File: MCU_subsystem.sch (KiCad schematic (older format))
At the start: 14 parts, among them U3 MX25R8035FZUIL0, U601 cc1352p, Y601 32.768kHz, Y602 48MHz

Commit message: relinked LED and BTN footprints. Need to make flash symbol again
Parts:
- U3: symbol FLASH:MX25R8035FZUIL0 -> UserMade-BB-Zigbee-Gateway-CAPE:MX25R8035FZUIL0
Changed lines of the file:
@@
 	2900 5950 2700 5950
 $Comp
-L FLASH:MX25R8035FZUIL0 U3
+L UserMade-BB-Zigbee-Gateway-CAPE:MX25R8035FZUIL0 U3
 U 1 1 615019E6
 P 4300 6700

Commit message: Recovered the .lib for flash symbol. Relinked in schematic
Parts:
- C26, C601, C602: symbol Device:C -> BeagleBone-Black-Cape-rescue:C-Device
- C603, C604: symbol pspice:CAP -> BeagleBone-Black-Cape-rescue:CAP-pspice
- R14, R15, R16, R17, R601: symbol Device:R_US -> BeagleBone-Black-Cape-rescue:R_US-Device
- U3: symbol UserMade-BB-Zigbee-Gateway-CAPE:MX25R8035FZUIL0 -> Flash_Usr:MX25R8035FZUIL0
- Y601: symbol Device:Crystal -> BeagleBone-Black-Cape-rescue:Crystal-Device
- Y602: symbol Device:Crystal_GND2 -> BeagleBone-Black-Cape-rescue:Crystal_GND2-Device
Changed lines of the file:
@@
 SKY_V1_20DBM
 $Comp
-L power:GND #PWR0602
+L BeagleBone-Black-Cape-rescue:GND-power #PWR0602
 U 1 1 614C8FCE
 P 2150 4200
@@
 	2750 4100 2650 4100
 $Comp
-L Device:R_US R601
+L BeagleBone-Black-Cape-rescue:R_US-Device R601
 U 1 1 614CB248
 P 1700 3650
@@
 Connection ~ 2000 3800
 $Comp
-L Device:C C602
+L BeagleBone-Black-Cape-rescue:C-Device C602
 U 1 1 614CF3BD
 P 2150 4050
@@
 Connection ~ 1700 3400
 $Comp
-L Device:C C601
+L BeagleBone-Black-Cape-rescue:C-Device C601
 U 1 1 614D5273
 P 2050 3000
@@
 $EndComp
 $Comp
-L power:GND #PWR0601
+L BeagleBone-Black-Cape-rescue:GND-power #PWR0601
 U 1 1 614D592A
 P 2050 3150
@@
 	1700 2850 2050 2850
 $Comp
-L power:GND #PWR0603
+L BeagleBone-Black-Cape-rescue:GND-power #PWR0603
 U 1 1 614DC14A
 P 3150 5100
@@
 	3400 5100 3400 5000
 $Comp
-L Device:Crystal Y?
+L BeagleBone-Black-Cape-rescue:Crystal-Device Y?
 U 1 1 614E7AAF
 P 7450 4000
@@
 $EndComp
 $Comp
-L Device:Crystal_GND2 Y?
+L BeagleBone-Black-Cape-rescue:Crystal_GND2-Device Y?
 U 1 1 614E7AB5
 P 8750 4300
@@
 $EndComp
 $Comp
-L pspice:CAP C?
+L BeagleBone-Black-Cape-rescue:CAP-pspice C?
 U 1 1 614E7ABB
 P 7100 4350
@@
 $EndComp
 $Comp
-L pspice:CAP C?
+L BeagleBone-Black-Cape-rescue:CAP-pspice C?
 U 1 1 614E7AC1
 P 7800 4350
@@
 	7800 4000 7800 4100
 $Comp
-L power:GND #PWR?
+L BeagleBone-Black-Cape-rescue:GND-power #PWR?
 U 1 1 614E7ACB
 P 8750 4600
@@
 $EndComp
 $Comp
-L power:GND #PWR?
+L BeagleBone-Black-Cape-rescue:GND-power #PWR?
 U 1 1 614E7AD1
 P 7800 4700
@@
 $EndComp
 $Comp
-L power:GND #PWR?
+L BeagleBone-Black-Cape-rescue:GND-power #PWR?
 U 1 1 614E7AD7
 P 7100 4700
@@
 Exact cap Value will need to be \ndetermined by measuring the board. \nThis will also affect the exact \ncrystal we end up getting.
 $Comp
-L power:GND #PWR0143
+L BeagleBone-Black-Cape-rescue:GND-power #PWR0143
 U 1 1 614D787A
 P 4500 7100
@@
 $EndComp
 $Comp
-L power:GND #PWR0144
+L BeagleBone-Black-Cape-rescue:GND-power #PWR0144
 U 1 1 614D8142
 P 5100 7100
@@
 MCU_VDD
 $Comp
-L Device:R_US R16
+L BeagleBone-Black-Cape-rescue:R_US-Device R16
 U 1 1 614D91BC
 P 3450 6100
@@
 	3200 5950 3450 5950
 $Comp
-L Device:R_US R17
+L BeagleBone-Black-Cape-rescue:R_US-Device R17
 U 1 1 614DDC0C
 P 4950 6100
@@
 $EndComp
 $Comp
-L Device:C C26
+L BeagleBone-Black-Cape-rescue:C-Device C26
 U 1 1 614E11ED
 P 5100 6950
@@
 	3700 6500 3800 6500
 $Comp
-L Device:R_US R14
+L BeagleBone-Black-Cape-rescue:R_US-Device R14
 U 1 1 614EF3D8
 P 2900 6300
@@
 $EndComp
 $Comp
-L Device:R_US R15
+L BeagleBone-Black-Cape-rescue:R_US-Device R15
 U 1 1 614F0C42
 P 3200 6300
@@
 	2900 5950 2700 5950
 $Comp
-L UserMade-BB-Zigbee-Gateway-CAPE:MX25R8035FZUIL0 U3
+L Flash_Usr:MX25R8035FZUIL0 U3
 U 1 1 615019E6
 P 4300 6700

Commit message: prepped for PSU subsystem placements
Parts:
- U602: renamed from U3; symbol Flash_Usr:MX25R8035FZUIL0 -> BeagleBone-Black-Cape-rescue:MX25R8035FZUIL0-Flash_Usr
- renumbered C26 to C603, C603 to C604, C604 to C605, R14 to R602, R15 to R603, R16 to R604, R17 to R605
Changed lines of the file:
@@
 P 7100 4350
 AR Path="/613805C9/614E7ABB" Ref="C?"  Part="1"
-AR Path="/614C2CA1/614E7ABB" Ref="C603"  Part="1"
-F 0 "C603" H 7278 4396 50  0000 L CNN
+AR Path="/614C2CA1/614E7ABB" Ref="C604"  Part="1"
+F 0 "C604" H 7278 4396 50  0000 L CNN
 F 1 "CAP" H 7278 4305 50  0000 L CNN
 F 2 "Capacitor_SMD:C_0805_2012Metric_Pad1.18x1.45mm_HandSolder" H 7100 4350 50  0001 C CNN
@@
 P 7800 4350
 AR Path="/613805C9/614E7AC1" Ref="C?"  Part="1"
-AR Path="/614C2CA1/614E7AC1" Ref="C604"  Part="1"
-F 0 "C604" H 7978 4396 50  0000 L CNN
+AR Path="/614C2CA1/614E7AC1" Ref="C605"  Part="1"
+F 0 "C605" H 7978 4396 50  0000 L CNN
 F 1 "CAP" H 7978 4305 50  0000 L CNN
 F 2 "Capacitor_SMD:C_0805_2012Metric_Pad1.18x1.45mm_HandSolder" H 7800 4350 50  0001 C CNN
@@
 P 8750 4600
 AR Path="/613805C9/614E7ACB" Ref="#PWR?"  Part="1"
-AR Path="/614C2CA1/614E7ACB" Ref="#PWR0606"  Part="1"
-F 0 "#PWR0606" H 8750 4350 50  0001 C CNN
+AR Path="/614C2CA1/614E7ACB" Ref="#PWR0608"  Part="1"
+F 0 "#PWR0608" H 8750 4350 50  0001 C CNN
 F 1 "GND" H 8755 4427 50  0000 C CNN
 F 2 "" H 8750 4600 50  0001 C CNN
@@
 P 7800 4700
 AR Path="/613805C9/614E7AD1" Ref="#PWR?"  Part="1"
-AR Path="/614C2CA1/614E7AD1" Ref="#PWR0605"  Part="1"
-F 0 "#PWR0605" H 7800 4450 50  0001 C CNN
+AR Path="/614C2CA1/614E7AD1" Ref="#PWR0607"  Part="1"
+F 0 "#PWR0607" H 7800 4450 50  0001 C CNN
 F 1 "GND" H 7805 4527 50  0000 C CNN
 F 2 "" H 7800 4700 50  0001 C CNN
@@
 P 7100 4700
 AR Path="/613805C9/614E7AD7" Ref="#PWR?"  Part="1"
-AR Path="/614C2CA1/614E7AD7" Ref="#PWR0604"  Part="1"
-F 0 "#PWR0604" H 7100 4450 50  0001 C CNN
+AR Path="/614C2CA1/614E7AD7" Ref="#PWR0606"  Part="1"
+F 0 "#PWR0606" H 7100 4450 50  0001 C CNN
 F 1 "GND" H 7105 4527 50  0000 C CNN
 F 2 "" H 7100 4700 50  0001 C CNN
@@
 Exact cap Value will need to be \ndetermined by measuring the board. \nThis will also affect the exact \ncrystal we end up getting.
 $Comp
-L BeagleBone-Black-Cape-rescue:GND-power #PWR0143
+L BeagleBone-Black-Cape-rescue:GND-power #PWR0604
 U 1 1 614D787A
 P 4500 7100
-F 0 "#PWR0143" H 4500 6850 50  0001 C CNN
+F 0 "#PWR0604" H 4500 6850 50  0001 C CNN
 F 1 "GND" H 4505 6927 50  0000 C CNN
 F 2 "" H 4500 7100 50  0001 C CNN
@@
 $EndComp
 $Comp
-L BeagleBone-Black-Cape-rescue:GND-power #PWR0144
+L BeagleBone-Black-Cape-rescue:GND-power #PWR0605
 U 1 1 614D8142
 P 5100 7100
-F 0 "#PWR0144" H 5100 6850 50  0001 C CNN
+F 0 "#PWR0605" H 5100 6850 50  0001 C CNN
 F 1 "GND" H 5105 6927 50  0000 C CNN
 F 2 "" H 5100 7100 50  0001 C CNN
@@
 MCU_VDD
 $Comp
-L BeagleBone-Black-Cape-rescue:R_US-Device R16
+L BeagleBone-Black-Cape-rescue:R_US-Device R604
 U 1 1 614D91BC
 P 3450 6100
-F 0 "R16" H 3518 6146 50  0000 L CNN
+F 0 "R604" H 3518 6146 50  0000 L CNN
 F 1 "2.2k" H 3518 6055 50  0000 L CNN
 F 2 "Resistor_SMD:R_0805_2012Metric_Pad1.20x1.40mm_HandSolder" V 3490 6090 50  0001 C CNN
@@
 	3200 5950 3450 5950
 $Comp
-L BeagleBone-Black-Cape-rescue:R_US-Device R17
+L BeagleBone-Black-Cape-rescue:R_US-Device R605
 U 1 1 614DDC0C
 P 4950 6100
-F 0 "R17" H 5018 6146 50  0000 L CNN
+F 0 "R605" H 5018 6146 50  0000 L CNN
 F 1 "0" H 5018 6055 50  0000 L CNN
 F 2 "Resistor_SMD:R_0805_2012Metric_Pad1.20x1.40mm_HandSolder" V 4990 6090 50  0001 C CNN
@@
 $EndComp
 $Comp
-L BeagleBone-Black-Cape-rescue:C-Device C26
+L BeagleBone-Black-Cape-rescue:C-Device C603
 U 1 1 614E11ED
 P 5100 6950
-F 0 "C26" H 5215 6996 50  0000 L CNN
+F 0 "C603" H 5215 6996 50  0000 L CNN
 F 1 "0.1u" H 5215 6905 50  0000 L CNN
 F 2 "Capacitor_SMD:C_0805_2012Metric_Pad1.18x1.45mm_HandSolder" H 5138 6800 50  0001 C CNN
@@
 	3700 6500 3800 6500
 $Comp
-L BeagleBone-Black-Cape-rescue:R_US-Device R14
+L BeagleBone-Black-Cape-rescue:R_US-Device R602
 U 1 1 614EF3D8
 P 2900 6300
-F 0 "R14" H 2968 6346 50  0000 L CNN
+F 0 "R602" H 2968 6346 50  0000 L CNN
 F 1 "DNS" H 2968 6255 50  0000 L CNN
 F 2 "Resistor_SMD:R_0805_2012Metric_Pad1.20x1.40mm_HandSolder" V 2940 6290 50  0001 C CNN
@@
 $EndComp
 $Comp
-L BeagleBone-Black-Cape-rescue:R_US-Device R15
+L BeagleBone-Black-Cape-rescue:R_US-Device R603
 U 1 1 614F0C42
 P 3200 6300
-F 0 "R15" H 3268 6346 50  0000 L CNN
+F 0 "R603" H 3268 6346 50  0000 L CNN
 F 1 "DNS" H 3268 6255 50  0000 L CNN
 F 2 "Resistor_SMD:R_0805_2012Metric_Pad1.20x1.40mm_HandSolder" V 3240 6290 50  0001 C CNN
@@
 	2900 5950 2700 5950
 $Comp
-L Flash_Usr:MX25R8035FZUIL0 U3
+L BeagleBone-Black-Cape-rescue:MX25R8035FZUIL0-Flash_Usr U?
 U 1 1 615019E6
 P 4300 6700
-F 0 "U3" H 4844 6746 50  0000 L CNN
+AR Path="/615019E6" Ref="U?"  Part="1"
+AR Path="/614C2CA1/615019E6" Ref="U602"  Part="1"
+F 0 "U602" H 4844 6746 50  0000 L CNN
 F 1 "MX25R8035FZUIL0" H 4844 6655 50  0000 L CNN
 F 2 "Package_SO:SOP-8_5.28x5.23mm_P1.27mm" H 4300 6100 50  0001 C CNN

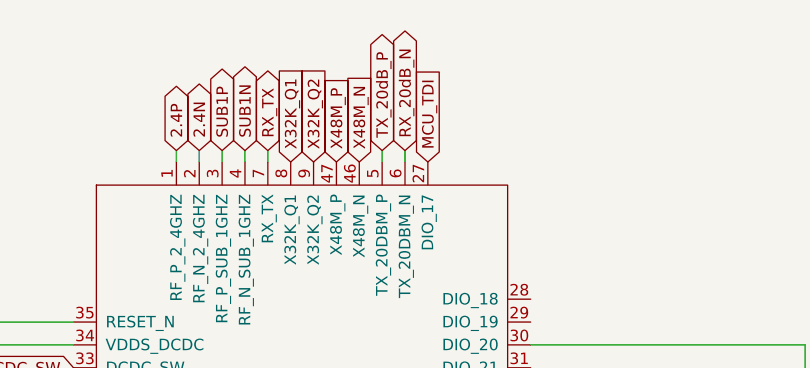
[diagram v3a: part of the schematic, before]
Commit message: Massive PCB/Schematic Update
The PCB has been completed, and the schematic has been updated to have the correct footprints
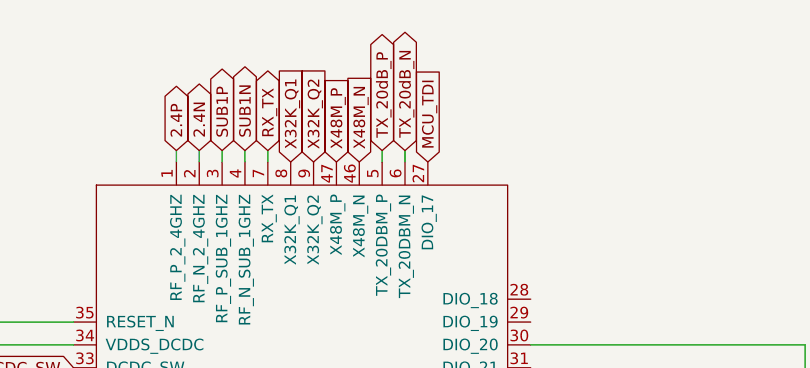
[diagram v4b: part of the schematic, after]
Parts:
- C601, C602: footprint Capacitor_SMD:C_0805_2012Metric_Pad1.18x1.45mm_HandSolder -> Capacitor_SMD:C_0402_1005Metric_Pad0.74x0.62mm_HandSolder
- R601: footprint Resistor_SMD:R_0805_2012Metric_Pad1.20x1.40mm_HandSolder -> Resistor_SMD:R_0402_1005Metric_Pad0.72x0.64mm_HandSolder
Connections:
- net RX_20dB_N renamed TX_20dB_N
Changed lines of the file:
@@
 	4200 2700 4200 2650
 Text GLabel 4300 2650 1    50   BiDi ~ 0
-RX_20dB_N
+TX_20dB_N
 Wire Wire Line
 	4300 2650 4300 2700
@@
 F 0 "R601" H 1768 3696 50  0000 L CNN
 F 1 "100k" H 1768 3605 50  0000 L CNN
-F 2 "Resistor_SMD:R_0805_2012Metric_Pad1.20x1.40mm_HandSolder" V 1740 3640 50  0001 C CNN
+F 2 "Resistor_SMD:R_0402_1005Metric_Pad0.72x0.64mm_HandSolder" V 1740 3640 50  0001 C CNN
 F 3 "~" H 1700 3650 50  0001 C CNN
 	1    1700 3650
@@
 F 0 "C602" H 2265 4096 50  0000 L CNN
 F 1 "1u" H 2265 4005 50  0000 L CNN
-F 2 "Capacitor_SMD:C_0805_2012Metric_Pad1.18x1.45mm_HandSolder" H 2188 3900 50  0001 C CNN
+F 2 "Capacitor_SMD:C_0402_1005Metric_Pad0.74x0.62mm_HandSolder" H 2188 3900 50  0001 C CNN
 F 3 "~" H 2150 4050 50  0001 C CNN
 	1    2150 4050
@@
 F 0 "C601" H 2165 3046 50  0000 L CNN
 F 1 "0.1u" H 2165 2955 50  0000 L CNN
-F 2 "Capacitor_SMD:C_0805_2012Metric_Pad1.18x1.45mm_HandSolder" H 2088 2850 50  0001 C CNN
+F 2 "Capacitor_SMD:C_0402_1005Metric_Pad0.74x0.62mm_HandSolder" H 2088 2850 50  0001 C CNN
 F 3 "~" H 2050 3000 50  0001 C CNN
 	1    2050 3000

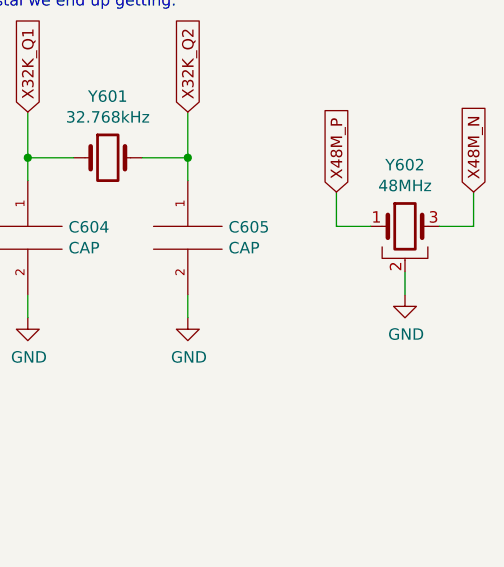
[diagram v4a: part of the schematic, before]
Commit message: Updated schematic and a symbol so that Y602 pad 4 was connected to the gnd net
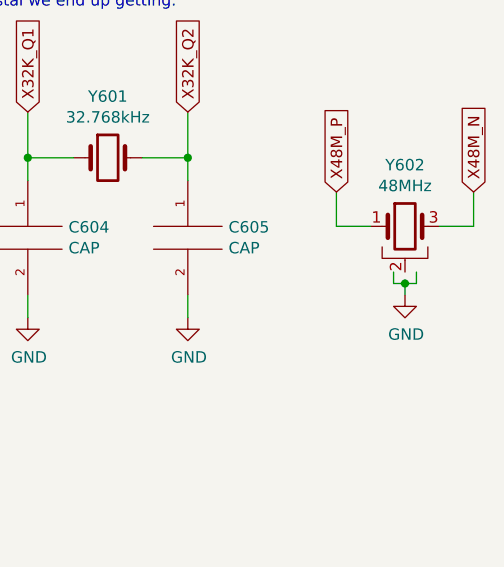
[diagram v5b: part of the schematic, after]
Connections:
- net GND: no longer Y602.2
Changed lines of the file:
@@
 	7800 4600 7800 4700
-Wire Wire Line
-	8750 4500 8750 4600
 Wire Wire Line
 	8600 4300 8450 4300
@@
 	1    0    0    -1
 $EndComp
+Wire Wire Line
+	8700 4500 8700 4550
+Wire Wire Line
+	8700 4550 8750 4550
+Wire Wire Line
+	8800 4550 8800 4500
+Wire Wire Line
+	8750 4600 8750 4550
+Connection ~ 8750 4550
+Wire Wire Line
+	8750 4550 8800 4550
 $EndSCHEMATC

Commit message: Apparently the schematic wasn't saved, and thus not commited. Here's that commit.
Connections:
- net GND: now also Y602.2
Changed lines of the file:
@@
 $EndComp
 Wire Wire Line
-	8700 4500 8700 4550
-Wire Wire Line
-	8700 4550 8750 4550
-Wire Wire Line
-	8800 4550 8800 4500
-Wire Wire Line
-	8750 4600 8750 4550
-Connection ~ 8750 4550
-Wire Wire Line
-	8750 4550 8800 4550
+	8750 4500 8750 4600
 $EndSCHEMATC

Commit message: lib update so it only includes user-made library
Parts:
- C601, C602, C603: symbol BeagleBone-Black-Cape-rescue:C-Device -> UserMade-BB-Zigbee-Gateway-CAPE:C-Device
- C604, C605: symbol BeagleBone-Black-Cape-rescue:CAP-pspice -> UserMade-BB-Zigbee-Gateway-CAPE:CAP-pspice
- R601, R602, R603, R604, R605: symbol BeagleBone-Black-Cape-rescue:R_US-Device -> UserMade-BB-Zigbee-Gateway-CAPE:R_US-Device
- U601: symbol cc1352:cc1352p -> UserMade-BB-Zigbee-Gateway-CAPE:cc1352p
- U602: symbol BeagleBone-Black-Cape-rescue:MX25R8035FZUIL0-Flash_Usr -> UserMade-BB-Zigbee-Gateway-CAPE:MX25R8035FZUIL0-Flash_Usr
- Y601: symbol BeagleBone-Black-Cape-rescue:Crystal-Device -> UserMade-BB-Zigbee-Gateway-CAPE:Crystal-Device
- Y602: symbol BeagleBone-Black-Cape-rescue:Crystal_GND2-Device -> UserMade-BB-Zigbee-Gateway-CAPE:Crystal_GND2-Device
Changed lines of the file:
@@
 	4850 4500 5000 4500
 $Comp
-L cc1352:cc1352p U?
+L UserMade-BB-Zigbee-Gateway-CAPE:cc1352p U?
 U 1 1 614C4674
 P 2950 4900
@@
 SKY_V1_20DBM
 $Comp
-L BeagleBone-Black-Cape-rescue:GND-power #PWR0602
+L UserMade-BB-Zigbee-Gateway-CAPE:GND-power #PWR0602
 U 1 1 614C8FCE
 P 2150 4200
@@
 	2750 4100 2650 4100
 $Comp
-L BeagleBone-Black-Cape-rescue:R_US-Device R601
+L UserMade-BB-Zigbee-Gateway-CAPE:R_US-Device R601
 U 1 1 614CB248
 P 1700 3650
@@
 Connection ~ 2000 3800
 $Comp
-L BeagleBone-Black-Cape-rescue:C-Device C602
+L UserMade-BB-Zigbee-Gateway-CAPE:C-Device C602
 U 1 1 614CF3BD
 P 2150 4050
@@
 Connection ~ 1700 3400
 $Comp
-L BeagleBone-Black-Cape-rescue:C-Device C601
+L UserMade-BB-Zigbee-Gateway-CAPE:C-Device C601
 U 1 1 614D5273
 P 2050 3000
@@
 $EndComp
 $Comp
-L BeagleBone-Black-Cape-rescue:GND-power #PWR0601
+L UserMade-BB-Zigbee-Gateway-CAPE:GND-power #PWR0601
 U 1 1 614D592A
 P 2050 3150
@@
 	1700 2850 2050 2850
 $Comp
-L BeagleBone-Black-Cape-rescue:GND-power #PWR0603
+L UserMade-BB-Zigbee-Gateway-CAPE:GND-power #PWR0603
 U 1 1 614DC14A
 P 3150 5100
@@
 	3400 5100 3400 5000
 $Comp
-L BeagleBone-Black-Cape-rescue:Crystal-Device Y?
+L UserMade-BB-Zigbee-Gateway-CAPE:Crystal-Device Y?
 U 1 1 614E7AAF
 P 7450 4000
@@
 $EndComp
 $Comp
-L BeagleBone-Black-Cape-rescue:Crystal_GND2-Device Y?
+L UserMade-BB-Zigbee-Gateway-CAPE:Crystal_GND2-Device Y?
 U 1 1 614E7AB5
 P 8750 4300
@@
 $EndComp
 $Comp
-L BeagleBone-Black-Cape-rescue:CAP-pspice C?
+L UserMade-BB-Zigbee-Gateway-CAPE:CAP-pspice C?
 U 1 1 614E7ABB
 P 7100 4350
@@
 $EndComp
 $Comp
-L BeagleBone-Black-Cape-rescue:CAP-pspice C?
+L UserMade-BB-Zigbee-Gateway-CAPE:CAP-pspice C?
 U 1 1 614E7AC1
 P 7800 4350
@@
 	7800 4000 7800 4100
 $Comp
-L BeagleBone-Black-Cape-rescue:GND-power #PWR?
+L UserMade-BB-Zigbee-Gateway-CAPE:GND-power #PWR?
 U 1 1 614E7ACB
 P 8750 4600
@@
 $EndComp
 $Comp
-L BeagleBone-Black-Cape-rescue:GND-power #PWR?
+L UserMade-BB-Zigbee-Gateway-CAPE:GND-power #PWR?
 U 1 1 614E7AD1
 P 7800 4700
@@
 $EndComp
 $Comp
-L BeagleBone-Black-Cape-rescue:GND-power #PWR?
+L UserMade-BB-Zigbee-Gateway-CAPE:GND-power #PWR?
 U 1 1 614E7AD7
 P 7100 4700
@@
 Exact cap Value will need to be \ndetermined by measuring the board. \nThis will also affect the exact \ncrystal we end up getting.
 $Comp
-L BeagleBone-Black-Cape-rescue:GND-power #PWR0604
+L UserMade-BB-Zigbee-Gateway-CAPE:GND-power #PWR0604
 U 1 1 614D787A
 P 4500 7100
@@
 $EndComp
 $Comp
-L BeagleBone-Black-Cape-rescue:GND-power #PWR0605
+L UserMade-BB-Zigbee-Gateway-CAPE:GND-power #PWR0605
 U 1 1 614D8142
 P 5100 7100
@@
 MCU_VDD
 $Comp
-L BeagleBone-Black-Cape-rescue:R_US-Device R604
+L UserMade-BB-Zigbee-Gateway-CAPE:R_US-Device R604
 U 1 1 614D91BC
 P 3450 6100
@@
 	3200 5950 3450 5950
 $Comp
-L BeagleBone-Black-Cape-rescue:R_US-Device R605
+L UserMade-BB-Zigbee-Gateway-CAPE:R_US-Device R605
 U 1 1 614DDC0C
 P 4950 6100
@@
 $EndComp
 $Comp
-L BeagleBone-Black-Cape-rescue:C-Device C603
+L UserMade-BB-Zigbee-Gateway-CAPE:C-Device C603
 U 1 1 614E11ED
 P 5100 6950
@@
 	3700 6500 3800 6500
 $Comp
-L BeagleBone-Black-Cape-rescue:R_US-Device R602
+L UserMade-BB-Zigbee-Gateway-CAPE:R_US-Device R602
 U 1 1 614EF3D8
 P 2900 6300
@@
 $EndComp
 $Comp
-L BeagleBone-Black-Cape-rescue:R_US-Device R603
+L UserMade-BB-Zigbee-Gateway-CAPE:R_US-Device R603
 U 1 1 614F0C42
 P 3200 6300
@@
 	2900 5950 2700 5950
 $Comp
-L BeagleBone-Black-Cape-rescue:MX25R8035FZUIL0-Flash_Usr U?
+L UserMade-BB-Zigbee-Gateway-CAPE:MX25R8035FZUIL0-Flash_Usr U?
 U 1 1 615019E6
 P 4300 6700

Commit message: final edits before it'll be untouched
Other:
- moved on the sheet: C603, C604, C605, R602, R603, R604, R605, U602, Y601, Y602
